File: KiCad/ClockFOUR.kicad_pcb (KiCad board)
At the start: 2 copper layers, 210 x 228 mm, 401 parts, among them P1 ICSP, P2 FTDI, P3 LDR_header, P4 Button_Header, P5 BARREL_JACK, SW1 SW_RST, U1 ATMEGA328P, U2 DS3231N, X1 CRYSTAL

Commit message: Layout changes
+ increased size of 5V traces
+ board notch around RTC battery
+ added breakout pins
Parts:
- added S5: CONN_1, PIN_ARRAY_1, F.Cu at (149.2, 85.2)
- added S6: CONN_1, PIN_ARRAY_1, F.Cu at (146.2, 85.2)
- added S7: CONN_1, PIN_ARRAY_1, F.Cu at (126.8, 85.2)
- added S8: CONN_1, PIN_ARRAY_1, F.Cu at (123.8, 85.2)
- added S9: CONN_1, PIN_ARRAY_1, F.Cu at (119.2, 85.2)
- moved P5 15.3 mm to (150.2, 265.8)
- moved BT1 2.50 mm to (84.0, 48.5)
- moved C9 2.50 mm to (98.2, 48.8)
- moved C1 0.75 mm to (138.2, 83.2)
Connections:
- U1 pad 1: (no net) -> /D3
- U1 pad 10: (no net) -> /D6
- U1 pad 11: (no net) -> /D7
- U1 pad 2: (no net) -> /D4
- U1 pad 9: (no net) -> /D5
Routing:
- net /MATRIX_PIN: track 119.3 -> 198.3 mm
- net /D7: track 0.00 -> 16.2 mm
- net /D6: track 0.00 -> 12.8 mm
- net /D3: track 0.00 -> 12.2 mm
- net GND: track 17.7 -> 6.91 mm, vias 1 -> 0
- net /D4: track 0.00 -> 10.7 mm
- net /D5: track 0.00 -> 10.4 mm
- net N-000003: track 13.1 -> 3.76 mm
- net 5V: track 3578.4 -> 3569.7 mm
- net /SDA: track 87.0 -> 86.2 mm
- net N-0000030: track 79.6 -> 80.4 mm
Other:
- outline, holes or cut-outs redrawn
- net class Power added: clearance 0.508, trace_width 0.508, via_dia 0.889, via_drill 0.635
- net class VCC added: clearance 0.254, trace_width 0.254, via_dia 0.889, via_drill 0.635

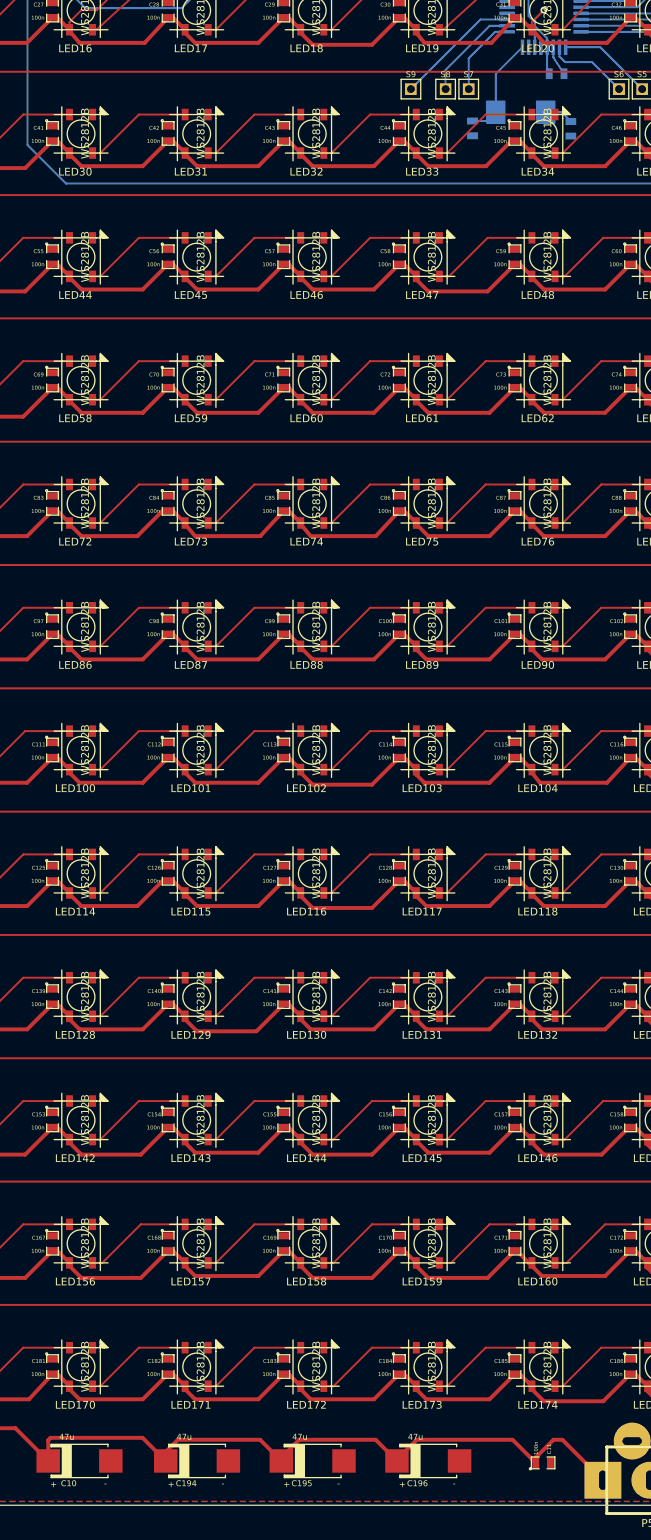
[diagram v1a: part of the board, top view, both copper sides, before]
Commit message: Layout updated
Fixed thin trace clearance error on ucontroller.
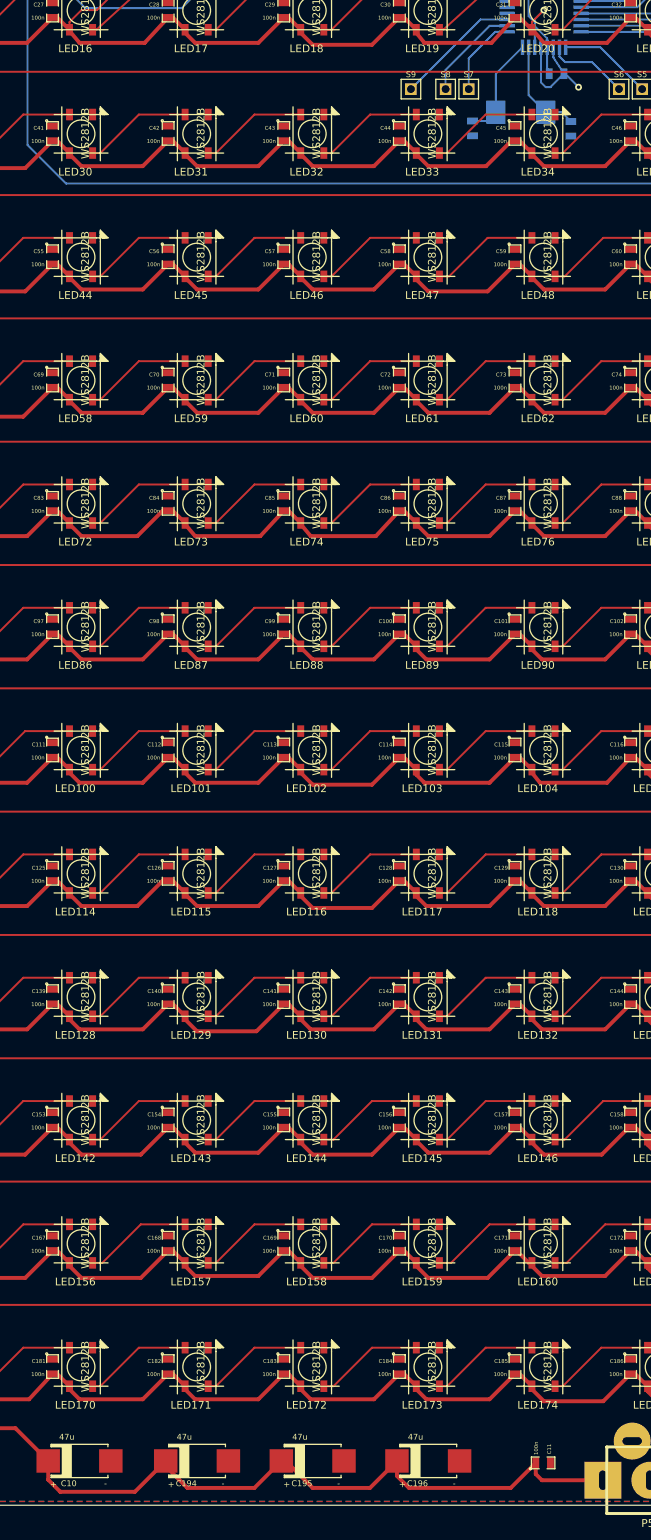
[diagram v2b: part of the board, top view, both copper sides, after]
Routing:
- net GND: track 6.91 -> 18.1 mm, vias 0 -> 1
- net N-000003: track 3.76 -> 13.1 mm
- net 5V: track 3569.7 -> 3570.5 mm
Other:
- net class Power: clearance 0.508 -> 0.254
- net class VCC removed
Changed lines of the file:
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@@
   (general
     (links 1005)
-    (no_connects 396)
-    (area 53.949999 33.449999 264.050001 269.050001)
+    (no_connects 0)
+    (area 53.899999 32.916999 264.100001 276.7)
     (thickness 1.6)
     (drawings 131)
-    (tracks 1943)
+    (tracks 1951)
     (zones 0)
     (modules 406)
@@
   (setup
     (last_trace_width 0.254)
+    (user_trace_width 0.254)
     (trace_clearance 0.254)
     (zone_clearance 0.508)
@@
   )
   (net_class Power ""
-    (clearance 0.508)
+    (clearance 0.254)
     (trace_width 0.508)
     (via_dia 0.889)
@@
     (add_net 5V)
   )
-  (net_class VCC ""
-    (clearance 0.254)
-    (trace_width 0.254)
-    (via_dia 0.889)
-    (via_drill 0.635)
-    (uvia_dia 0.508)
-    (uvia_drill 0.127)
-  )
   (module SIL-2 (layer F.Cu)
     (at 150.75 44.75)
@@
   (segment (start 221.75 73.5) (end 221.75 47.25) (width 0.254) (layer B.Cu) (net 31))
   (segment (start 219.22308 77.02692) (end 221.75 73.5) (width 0.254) (layer B.Cu) (net 31))
-  (segment (start 135.4475 263.5) (end 135.4475 262.8025) (width 0.508) (layer F.Cu) (net 32))
-  (segment (start 138.904 260.5) (end 144.154 265.75) (width 0.508) (layer F.Cu) (net 32))
-  (segment (start 137.75 260.5) (end 138.904 260.5) (width 0.508) (layer F.Cu) (net 32))
-  (segment (start 135.4475 262.8025) (end 137.75 260.5) (width 0.508) (layer F.Cu) (net 32))
+  (segment (start 117.436 263.25) (end 117.436 265.186) (width 0.508) (layer F.Cu) (net 32))
+  (segment (start 132.1975 266.75) (end 135.4475 263.5) (width 0.508) (layer F.Cu) (net 32))
+  (segment (start 119 266.75) (end 132.1975 266.75) (width 0.508) (layer F.Cu) (net 32))
+  (segment (start 117.436 265.186) (end 119 266.75) (width 0.508) (layer F.Cu) (net 32))
+  (segment (start 102.436 263.25) (end 103 263.25) (width 0.508) (layer F.Cu) (net 32))
+  (segment (start 113.936 266.75) (end 117.436 263.25) (width 0.508) (layer F.Cu) (net 32))
+  (segment (start 106.5 266.75) (end 113.936 266.75) (width 0.508) (layer F.Cu) (net 32))
+  (segment (start 103 263.25) (end 106.5 266.75) (width 0.508) (layer F.Cu) (net 32))
+  (segment (start 87.436 263.25) (end 87.436 263.936) (width 0.508) (layer F.Cu) (net 32))
+  (segment (start 98.936 266.75) (end 102.436 263.25) (width 0.508) (layer F.Cu) (net 32))
+  (segment (start 90.25 266.75) (end 98.936 266.75) (width 0.508) (layer F.Cu) (net 32))
+  (segment (start 87.436 263.936) (end 90.25 266.75) (width 0.508) (layer F.Cu) (net 32))
+  (segment (start 72.186 263.25) (end 72.186 265.686) (width 0.508) (layer F.Cu) (net 32))
+  (segment (start 83.436 267.25) (end 87.436 263.25) (width 0.508) (layer F.Cu) (net 32))
+  (segment (start 73.75 267.25) (end 83.436 267.25) (width 0.508) (layer F.Cu) (net 32))
+  (segment (start 72.186 265.686) (end 73.75 267.25) (width 0.508) (layer F.Cu) (net 32))
+  (segment (start 135.4475 263.5) (end 135.4475 264.9475) (width 0.508) (layer F.Cu) (net 32))
+  (segment (start 136.25 265.75) (end 144.154 265.75) (width 0.508) (layer F.Cu) (net 32))
+  (segment (start 135.4475 264.9475) (end 136.25 265.75) (width 0.508) (layer F.Cu) (net 32))
+  (segment (start 135.32398 79.81584) (end 135.32398 77.07398) (width 0.254) (layer B.Cu) (net 32))
+  (segment (start 135.32398 76.57398) (end 135.32398 76.17602) (width 0.254) (layer B.Cu) (net 32))
+  (segment (start 134.95 76.55) (end 136.5 75) (width 0.254) (layer F.Cu) (net 32))
+  (via (at 136.5 75) (size 0.889) (layers F.Cu B.Cu) (net 32))
+  (segment (start 134.95 76.55) (end 134.95 77.55) (width 0.254) (layer F.Cu) (net 32))
+  (segment (start 135.32398 76.17602) (end 136.5 75) (width 0.254) (layer B.Cu) (net 32))
   (segment (start 132.75 123.9525) (end 133.3525 123.9525) (width 0.508) (layer F.Cu) (net 32))
   (segment (start 133.3525 123.9525) (end 134.95 125.55) (width 0.508) (layer F.Cu) (net 32))
@@
   (segment (start 55.75 91) (end 55.75 77.9525) (width 0.508) (layer F.Cu) (net 32))
   (segment (start 56.7025 91.9525) (end 55.75 91) (width 0.508) (layer F.Cu) (net 32))
-  (segment (start 117.436 263.25) (end 117.436 263.064) (width 0.508) (layer F.Cu) (net 32))
-  (segment (start 132.4475 260.5) (end 135.4475 263.5) (width 0.508) (layer F.Cu) (net 32))
-  (segment (start 120 260.5) (end 132.4475 260.5) (width 0.508) (layer F.Cu) (net 32))
-  (segment (start 117.436 263.064) (end 120 260.5) (width 0.508) (layer F.Cu) (net 32))
-  (segment (start 102.436 263.25) (end 102.436 262.814) (width 0.508) (layer F.Cu) (net 32))
-  (segment (start 114.686 260.5) (end 117.436 263.25) (width 0.508) (layer F.Cu) (net 32))
-  (segment (start 104.75 260.5) (end 114.686 260.5) (width 0.508) (layer F.Cu) (net 32))
-  (segment (start 102.436 262.814) (end 104.75 260.5) (width 0.508) (layer F.Cu) (net 32))
-  (segment (start 87.436 263.25) (end 87.436 262.064) (width 0.508) (layer F.Cu) (net 32))
-  (segment (start 99.686 260.5) (end 102.436 263.25) (width 0.508) (layer F.Cu) (net 32))
-  (segment (start 89 260.5) (end 99.686 260.5) (width 0.508) (layer F.Cu) (net 32))
-  (segment (start 87.436 262.064) (end 89 260.5) (width 0.508) (layer F.Cu) (net 32))
-  (segment (start 72.186 263.25) (end 72.186 260.564) (width 0.508) (layer F.Cu) (net 32))
-  (segment (start 84.436 260.25) (end 87.436 263.25) (width 0.508) (layer F.Cu) (net 32))
-  (segment (start 72.5 260.25) (end 84.436 260.25) (width 0.508) (layer F.Cu) (net 32))
-  (segment (start 72.186 260.564) (end 72.5 260.25) (width 0.508) (layer F.Cu) (net 32))
   (segment (start 57.75 251.9525) (end 57.75 258.75) (width 0.508) (layer F.Cu) (net 32))
   (segment (start 67.936 259) (end 72.186 263.25) (width 0.508) (layer F.Cu) (net 32))
@@
   (segment (start 136.92418 79.81584) (end 136.92418 78.67418) (width 0.254) (layer B.Cu) (net 32))
   (segment (start 136.92418 78.67418) (end 135.32398 77.07398) (width 0.254) (layer B.Cu) (net 32))
-  (segment (start 135.32398 79.81584) (end 135.32398 77.07398) (width 0.254) (layer B.Cu) (net 32))
   (segment (start 135.32398 77.07398) (end 135.32398 76.57398) (width 0.254) (layer B.Cu) (net 32))
-  (segment (start 135.32398 76.57398) (end 135.32398 76.17602) (width 0.254) (layer B.Cu) (net 32))
-  (segment (start 135.32398 76.17602) (end 136.5 75) (width 0.254) (layer B.Cu) (net 32))
-  (segment (start 134.95 76.55) (end 134.95 77.55) (width 0.254) (layer F.Cu) (net 32))
-  (via (at 136.5 75) (size 0.889) (layers F.Cu B.Cu) (net 32))
-  (segment (start 134.95 76.55) (end 136.5 75) (width 0.254) (layer F.Cu) (net 32))
   (segment (start 79.9475 72) (end 79.9475 71.0525) (width 0.254) (layer B.Cu) (net 32))
   (segment (start 80.75 70.25) (end 83.25 70.25) (width 0.254) (layer B.Cu) (net 32))
@@
   (segment (start 166.5 63.1) (end 166.5 63.25) (width 0.254) (layer F.Cu) (net 32))
   (segment (start 166.5 63.25) (end 174 63.25) (width 0.508) (layer F.Cu) (net 32))
+  (segment (start 139.1025 83.25) (end 139.25 83.25) (width 0.254) (layer B.Cu) (net 33))
+  (via (at 141 85) (size 0.889) (layers F.Cu B.Cu) (net 33))
+  (segment (start 139.25 83.25) (end 141 85) (width 0.254) (layer B.Cu) (net 33))
+  (segment (start 136.12408 79.81584) (end 136.12408 84.37408) (width 0.254) (layer B.Cu) (net 33))
+  (segment (start 137.3525 85) (end 139.1025 83.25) (width 0.254) (layer B.Cu) (net 33))
+  (segment (start 136.75 85) (end 137.3525 85) (width 0.254) (layer B.Cu) (net 33))
+  (segment (start 136.12408 84.37408) (end 136.75 85) (width 0.254) (layer B.Cu) (net 33))
   (segment (start 136.9318 70.2502) (end 136.9318 67.4207) (width 0.254) (layer B.Cu) (net 33))
   (segment (start 136.9318 67.4207) (end 137.1025 67.25) (width 0.254) (layer B.Cu) (net 33))
@@
   (segment (start 158.95 248.55) (end 164.95 248.55) (width 0.254) (layer F.Cu) (net 158))
   (segment (start 153.95 253.55) (end 158.95 248.55) (width 0.254) (layer F.Cu) (net 158))
+  (segment (start 134.52388 79.81584) (end 134.52388 86.03538) (width 0.254) (layer B.Cu) (net 159))
+  (segment (start 134.52388 86.03538) (end 136.7385 88.25) (width 0.254) (layer B.Cu) (net 159))
   (segment (start 136.7385 88.25) (end 138.8025 88.25) (width 0.254) (layer B.Cu) (net 159))
   (segment (start 138.8025 88.25) (end 140 89.4475) (width 0.254) (layer B.Cu) (net 159))
